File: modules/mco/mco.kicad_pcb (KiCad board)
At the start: 2 copper layers, 30.5 x 68.6 mm, 22 parts, among them U1 ATtiny1616-M, U3 MCP6002-xSN

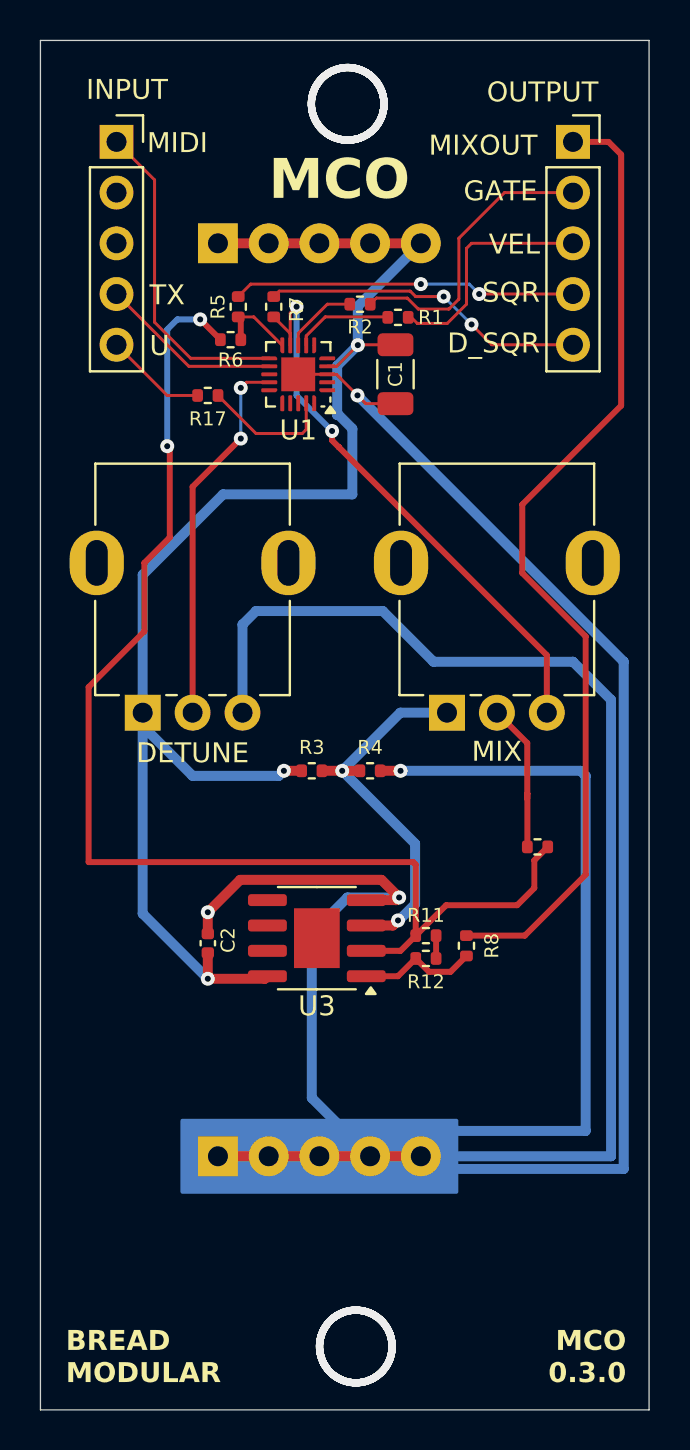
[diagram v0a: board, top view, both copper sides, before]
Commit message: mco: Add MIDI THRU support
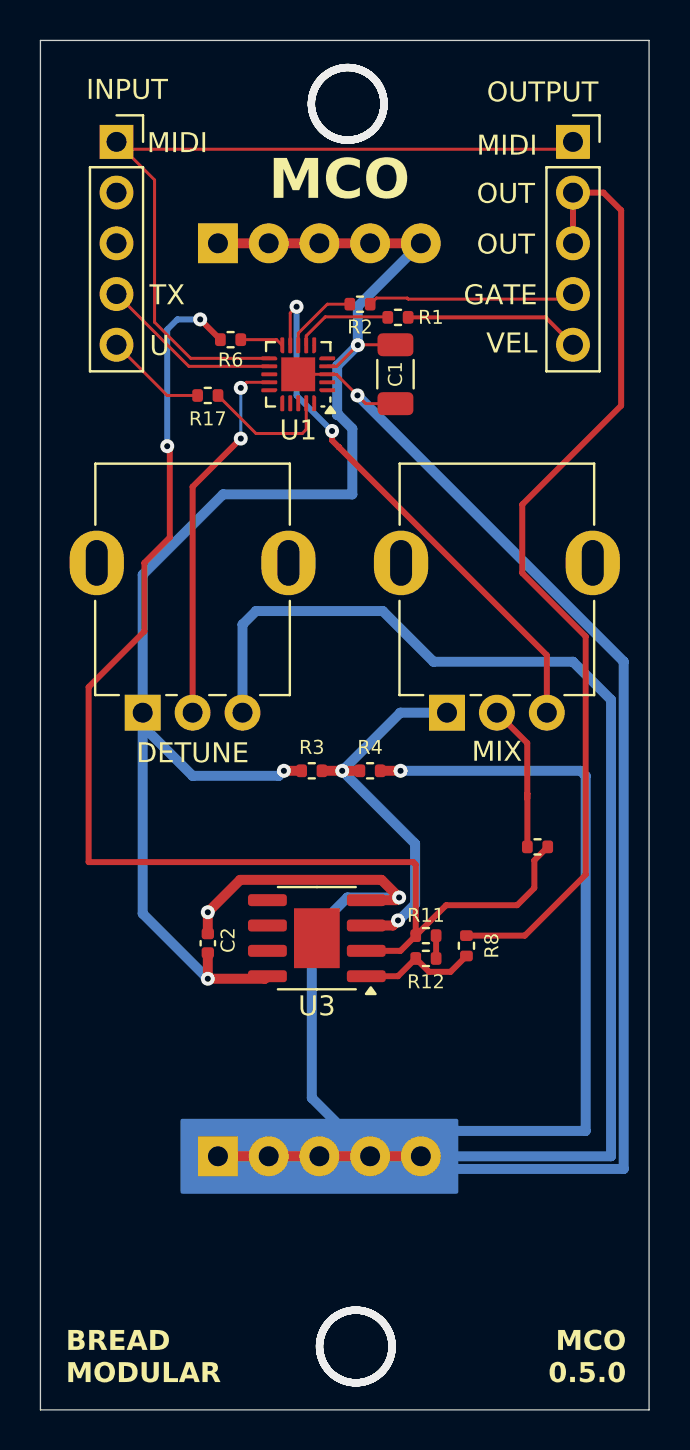
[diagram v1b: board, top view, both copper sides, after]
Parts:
- removed R5, R7: 1k, Resistor_SMD:R_0402_1005Metric
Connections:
- OUTPUT1 pad 1: MIX_OUT -> MIDI
- OUTPUT1 pad 2: GATE -> MIX_OUT
- OUTPUT1 pad 3: VELOCITY -> MIX_OUT
- OUTPUT1 pad 4: SQUARE_OUT -> GATE
- OUTPUT1 pad 5: DETUNED_OUT -> VELOCITY
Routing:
- net MIDI: track 16.3 -> 39.5 mm
- net SQUARE_OUT: track 17.2 -> 0.00 mm, vias 2 -> 0
- net DETUNED_OUT: track 16.2 -> 0.00 mm, vias 2 -> 0
- net GATE: track 14.7 -> 10.4 mm
- net VELOCITY: track 11.7 -> 8.82 mm
- net FUNDAMENTAL_TONE: track 3.99 -> 2.19 mm
- net DETUNED_TONE: track 29.4 -> 27.6 mm
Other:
- board text added: "MCO 0.5.0"
- board text added: "OUT"
- board text removed: "D_SQR"
- board text removed: "MCO 0.3.0"
- board text removed: "MIXOUT"
- board text removed: "SQR"

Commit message: mco_1.0.0
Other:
- board text added: "MCO 1.0.0"
- board text removed: "MCO 0.5.0"
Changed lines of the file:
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@@
 		)
 	)
-	(gr_text "MCO\n0.5.0"
+	(gr_text "MCO\n1.0.0"
 		(at 76.327 107.95 0)
 		(layer "F.SilkS")

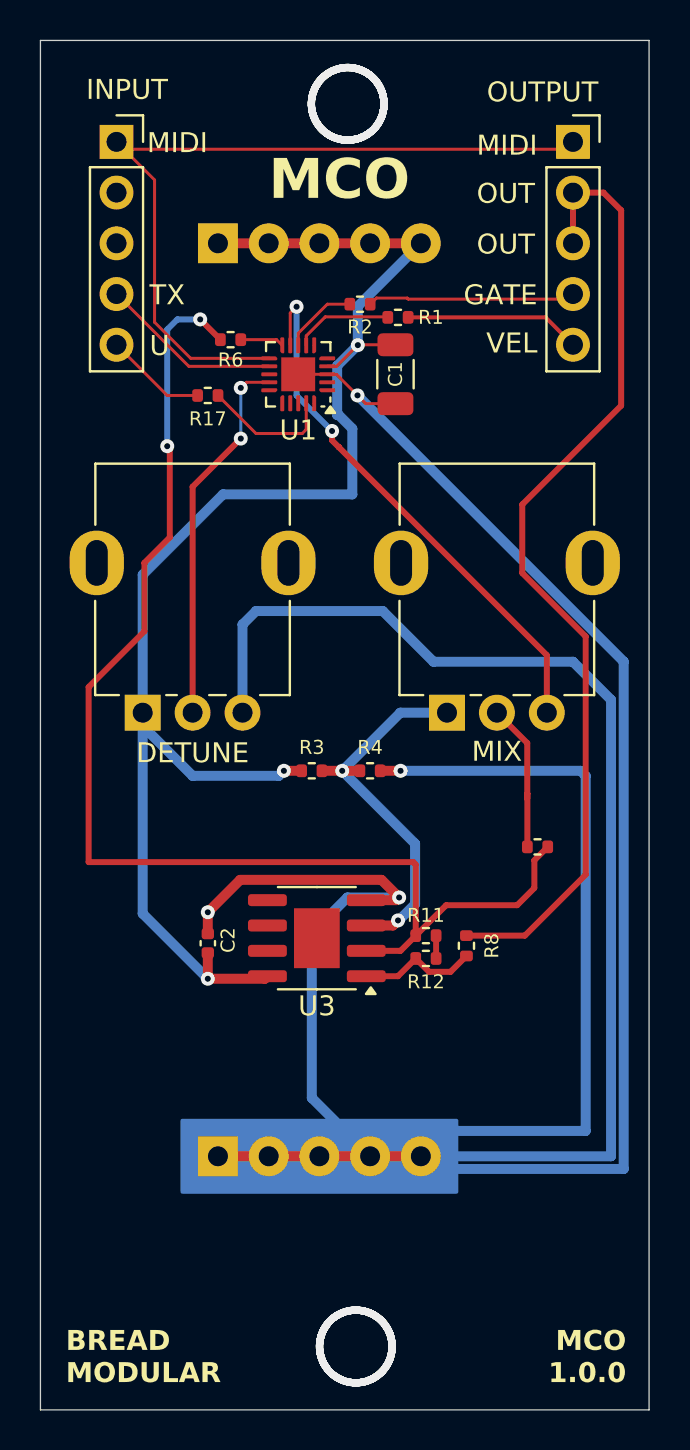
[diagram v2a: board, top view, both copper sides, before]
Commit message: mco: update footprints of pots
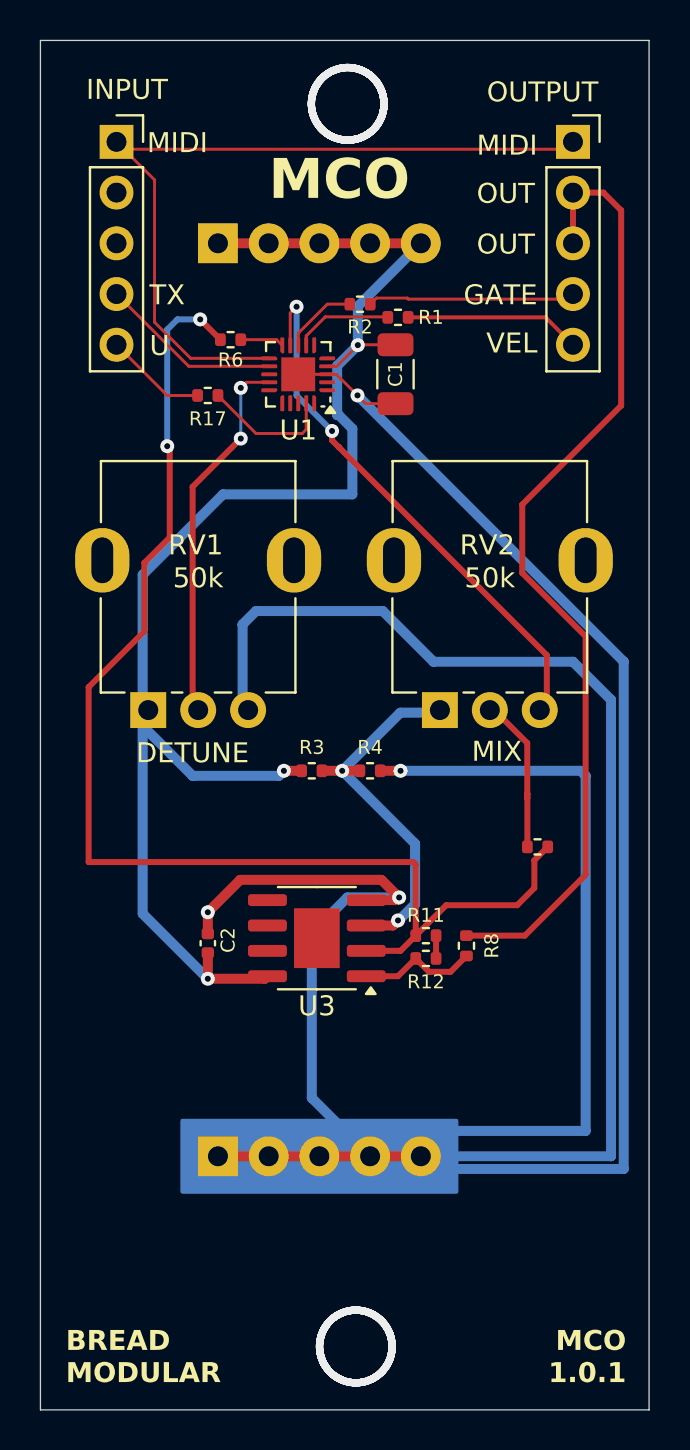
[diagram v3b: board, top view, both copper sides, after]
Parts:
- moved RV1 7.69 mm to (55.0, 67.2), turned to 0 degrees
- moved RV2 7.48 mm to (69.6, 67.2), turned to 0 degrees
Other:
- board text added: "MCO 1.0.1"
- board text removed: "MCO 1.0.0"
